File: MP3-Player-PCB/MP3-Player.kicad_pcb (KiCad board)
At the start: 4 copper layers, 50 x 50 mm, 113 parts, among them J101 Conn_ARM_SWD_TagConnect_TC2030, J201 Conn_01x02_Socket, J202 USB_C_Receptacle_USB2.0_16P, J301 Micro_SD_Card_Det1, Q301 AO3401A, Q302 2N7002H, Q303 AO3401A, Q304 AO3401A, Q305 2N7002H, SW301 1-1825910-4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

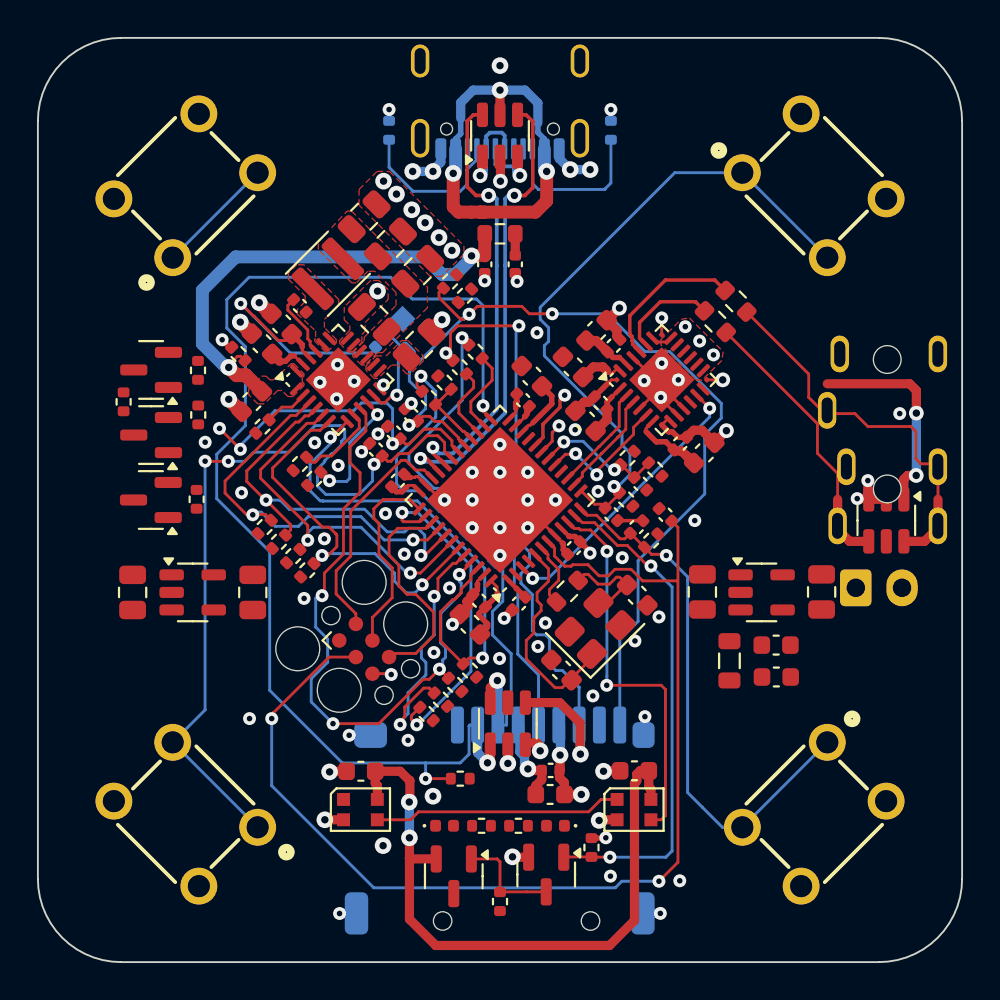
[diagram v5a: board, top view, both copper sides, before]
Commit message: Changing JST connector footprint to fit next to usb
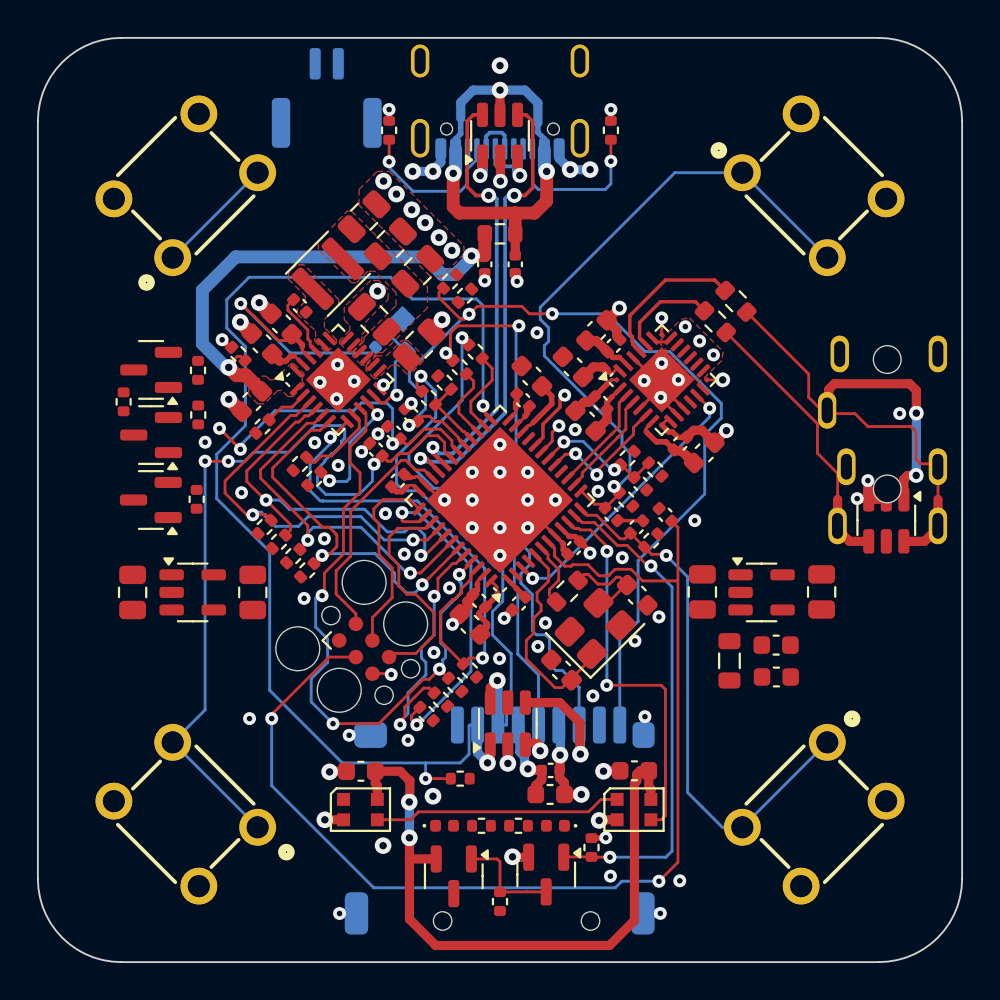
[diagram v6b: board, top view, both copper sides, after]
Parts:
- J201: footprint Connector_JST:JST_EH_S2B-EH_1x02_P2.50mm_Horizontal -> Connector_JST:JST_GH_SM02B-GHS-TB_1x02-1MP_P1.25mm_Horizontal
- R205, R206: moved to F.Cu
- moved J201 39.0 mm to (115.6, 103.2), turned to 180 degrees
- turned C214 to -90 degrees
- turned C215 to -90 degrees
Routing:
- net +VUSB: track 24.2 -> 25.2 mm
- net AUDIO_JACK_DET: track 29.3 -> 30.1 mm
- net /Power/USB_CON_CC2: track 8.75 -> 8.77 mm, vias 0 -> 1
- net /Power/USB_CON_CC1: vias 0 -> 1

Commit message: Routed VBAT power trace in 3rd layer
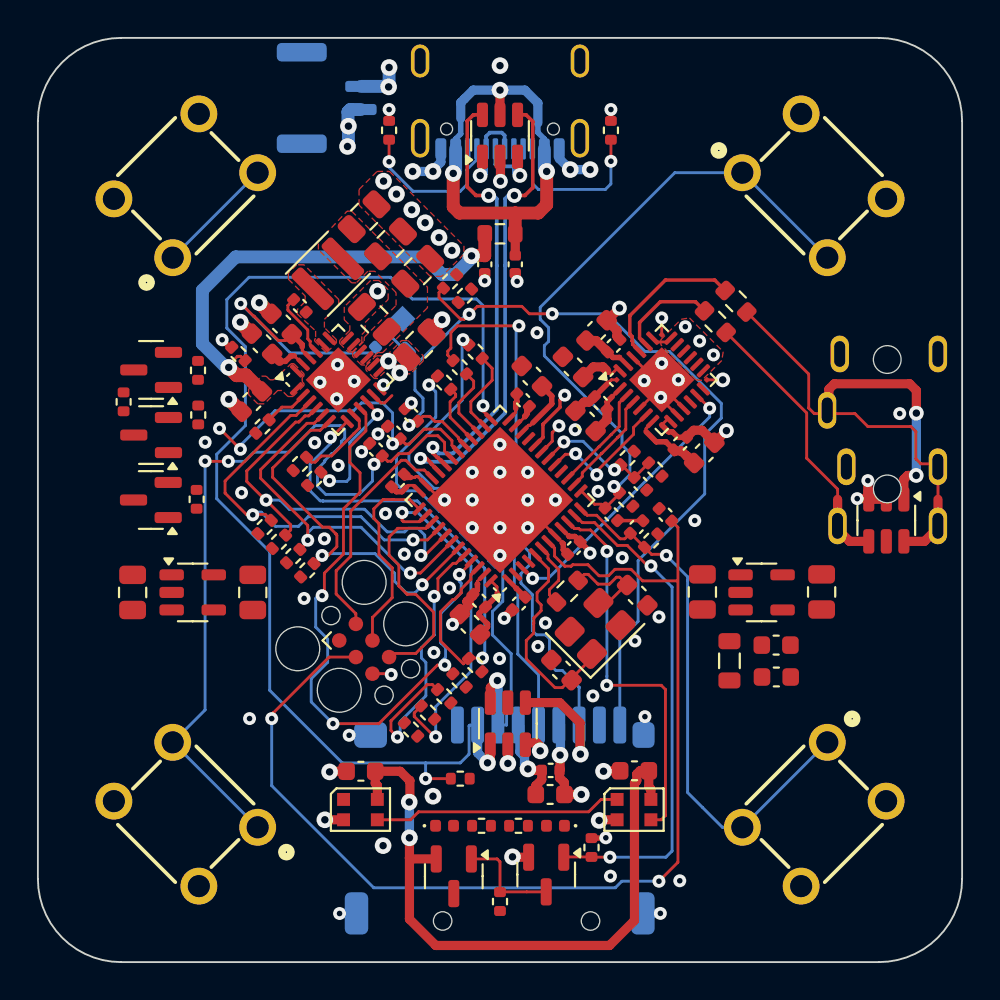
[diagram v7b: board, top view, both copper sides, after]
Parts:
- moved R302 18.9 mm to (120.2, 137.4), turned to 135 degrees
- moved R305 1.17 mm to (122.0, 118.7)
- moved R213 0.41 mm to (123.7, 133.9)
- moved R215 0.34 mm to (122.8, 134.8)
- moved R101 0.25 mm to (122.0, 135.6)
- moved R406 0.11 mm to (121.1, 136.5)
- turned J201 to 90 degrees
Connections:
- R302 pad 2: SD_CARD_MOSI -> /Peripherals/SD_CARD_MOSI_PIN
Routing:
- net /Power/BAT_TS: track 6.85 -> 3.81 mm, vias 1 -> 0
- net +VBAT: track 0.00 -> 2.66 mm, vias 0 -> 4
- net GND: track 69.6 -> 72.2 mm, vias 98 -> 99
- net /MCU/BOOT: track 14.1 -> 16.4 mm
- net AUDIO_JACK_DET: track 30.1 -> 31.3 mm
- net /Peripherals/SD_CARD_MOSI_PIN: track 29.4 -> 28.5 mm
- net SD_CARD_MOSI: track 3.91 -> 3.39 mm
- net SD_CARD_NCD: track 50.7 -> 50.2 mm
- net /Peripherals/SD_CARD_MISO_PIN: track 35.7 -> 36.2 mm, vias 3 -> 2
- added copper zone on In2.Cu, net +VBAT

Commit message: Finished signal routing for charger ic
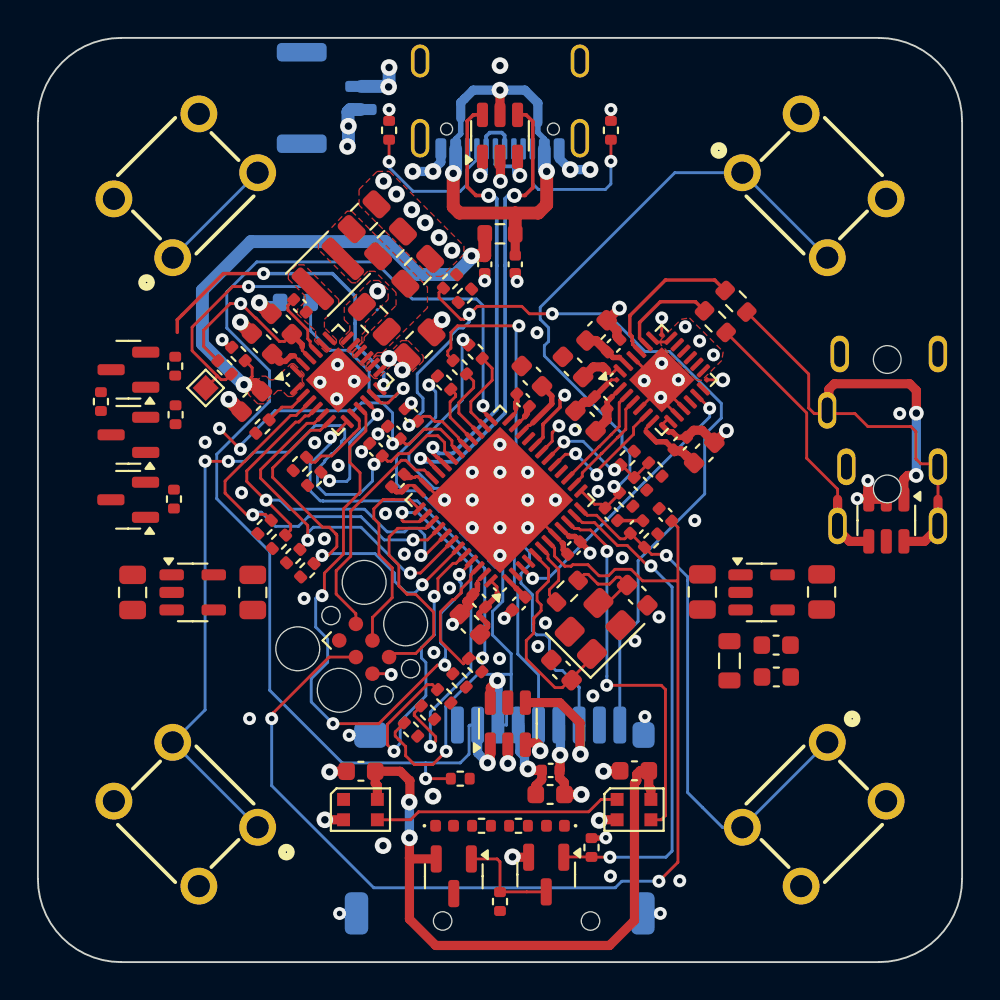
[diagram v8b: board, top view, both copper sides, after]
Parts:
- R207, TP201: moved to F.Cu
- moved TP201 11.3 mm to (109.1, 118.9), turned to 135 degrees
- moved R207 8.65 mm to (110.1, 117.8), turned to -45 degrees
- moved TH201 6.89 mm to (113.9, 114.3), turned to 180 degrees
- moved R314 1.25 mm to (107.4, 117.8)
- moved Q304 1.23 mm to (104.9, 121.5)
- moved Q305 1.23 mm to (104.9, 118.0)
- moved R313 1.23 mm to (107.4, 125.0)
- moved R315 1.23 mm to (103.4, 119.7)
- moved Q303 1.23 mm to (104.9, 125.0)
- moved R309 1.23 mm to (107.4, 120.4)
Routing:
- net /Power/BAT_TS: track 3.81 -> 24.0 mm, vias 0 -> 2
- net BAT_QON: track 0.31 -> 17.6 mm, vias 1 -> 2
- net /Peripherals/SD_CARD_MOSI_PIN: track 28.5 -> 40.1 mm, vias 2 -> 3
- net /Power/BAT_REGN: track 14.0 -> 10.0 mm
- net SD_CARD_NCS: track 64.9 -> 66.9 mm
- net /MCU/BOOT: track 16.4 -> 17.8 mm
- net AUDIO_JACK_DET: track 31.3 -> 32.6 mm
- net GND: track 72.2 -> 73.4 mm
- net +VUSB_FILT: track 26.8 -> 27.8 mm
